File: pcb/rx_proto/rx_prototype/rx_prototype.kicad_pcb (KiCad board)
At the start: 10 copper layers, 3 parts, among them U1 nice_nano, U4 MCP6004, U5 MCP6004

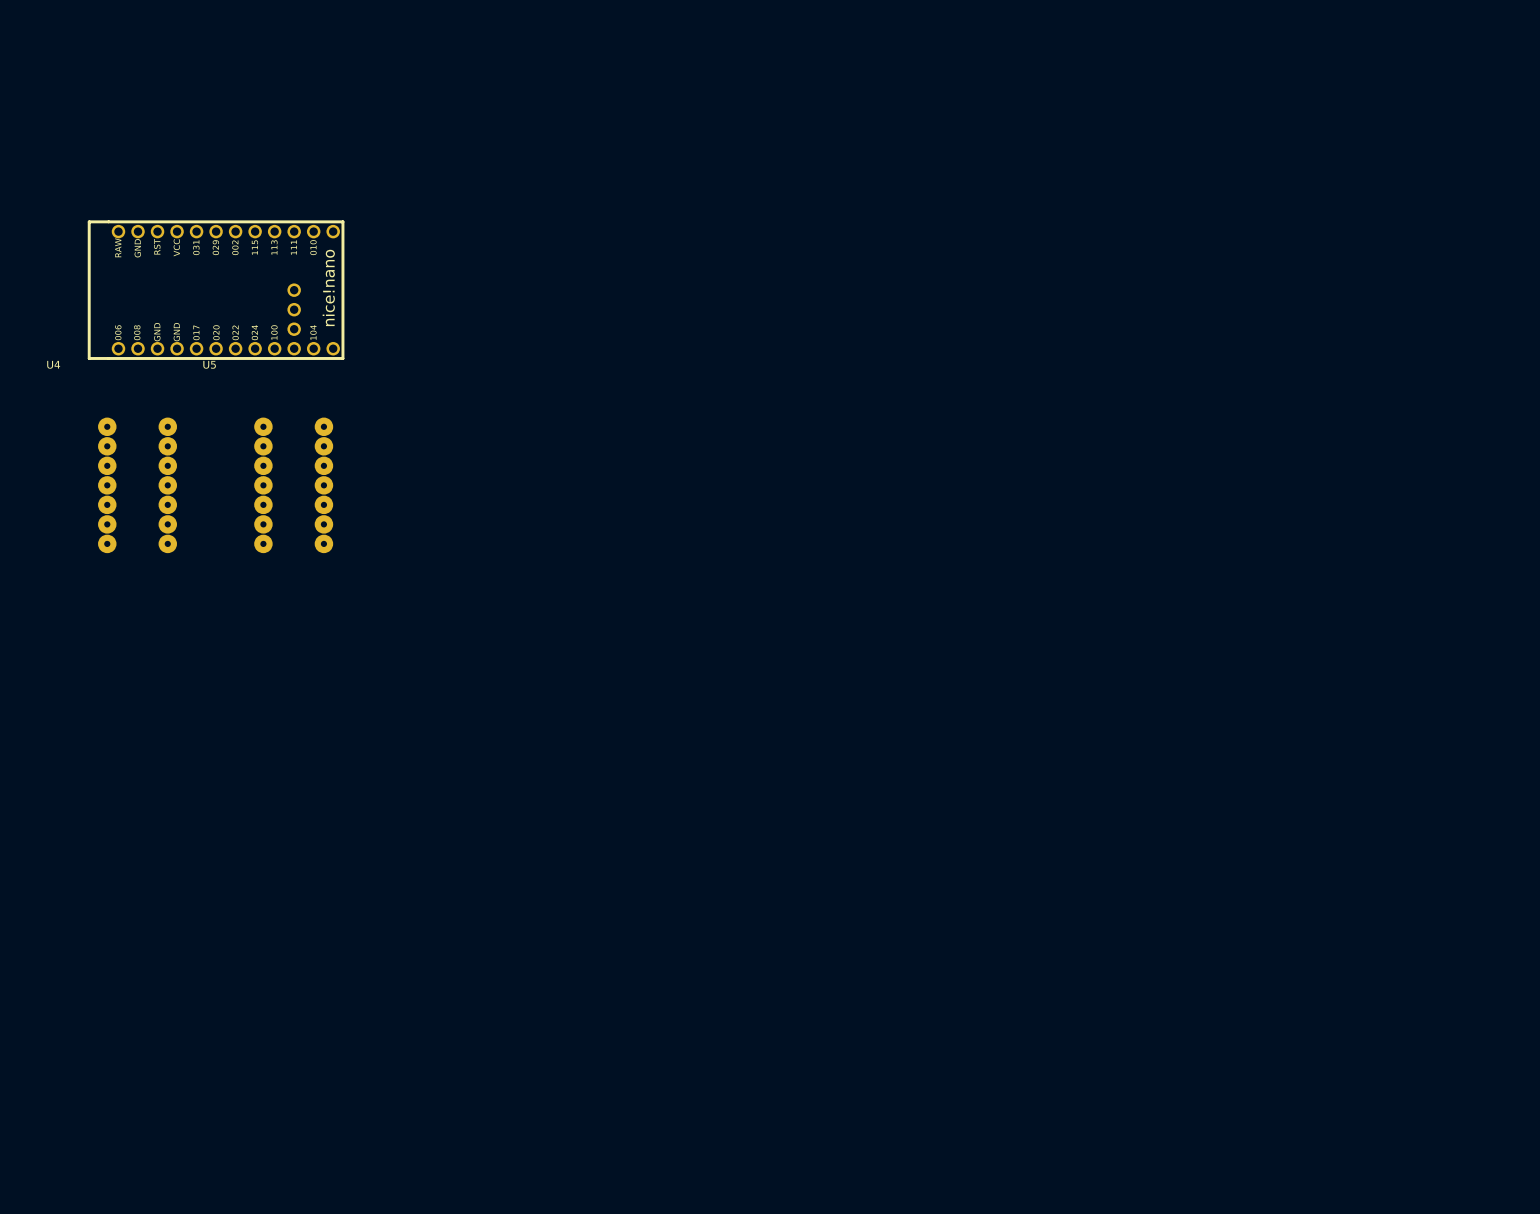
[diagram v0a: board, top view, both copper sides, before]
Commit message: Update perfboard layout
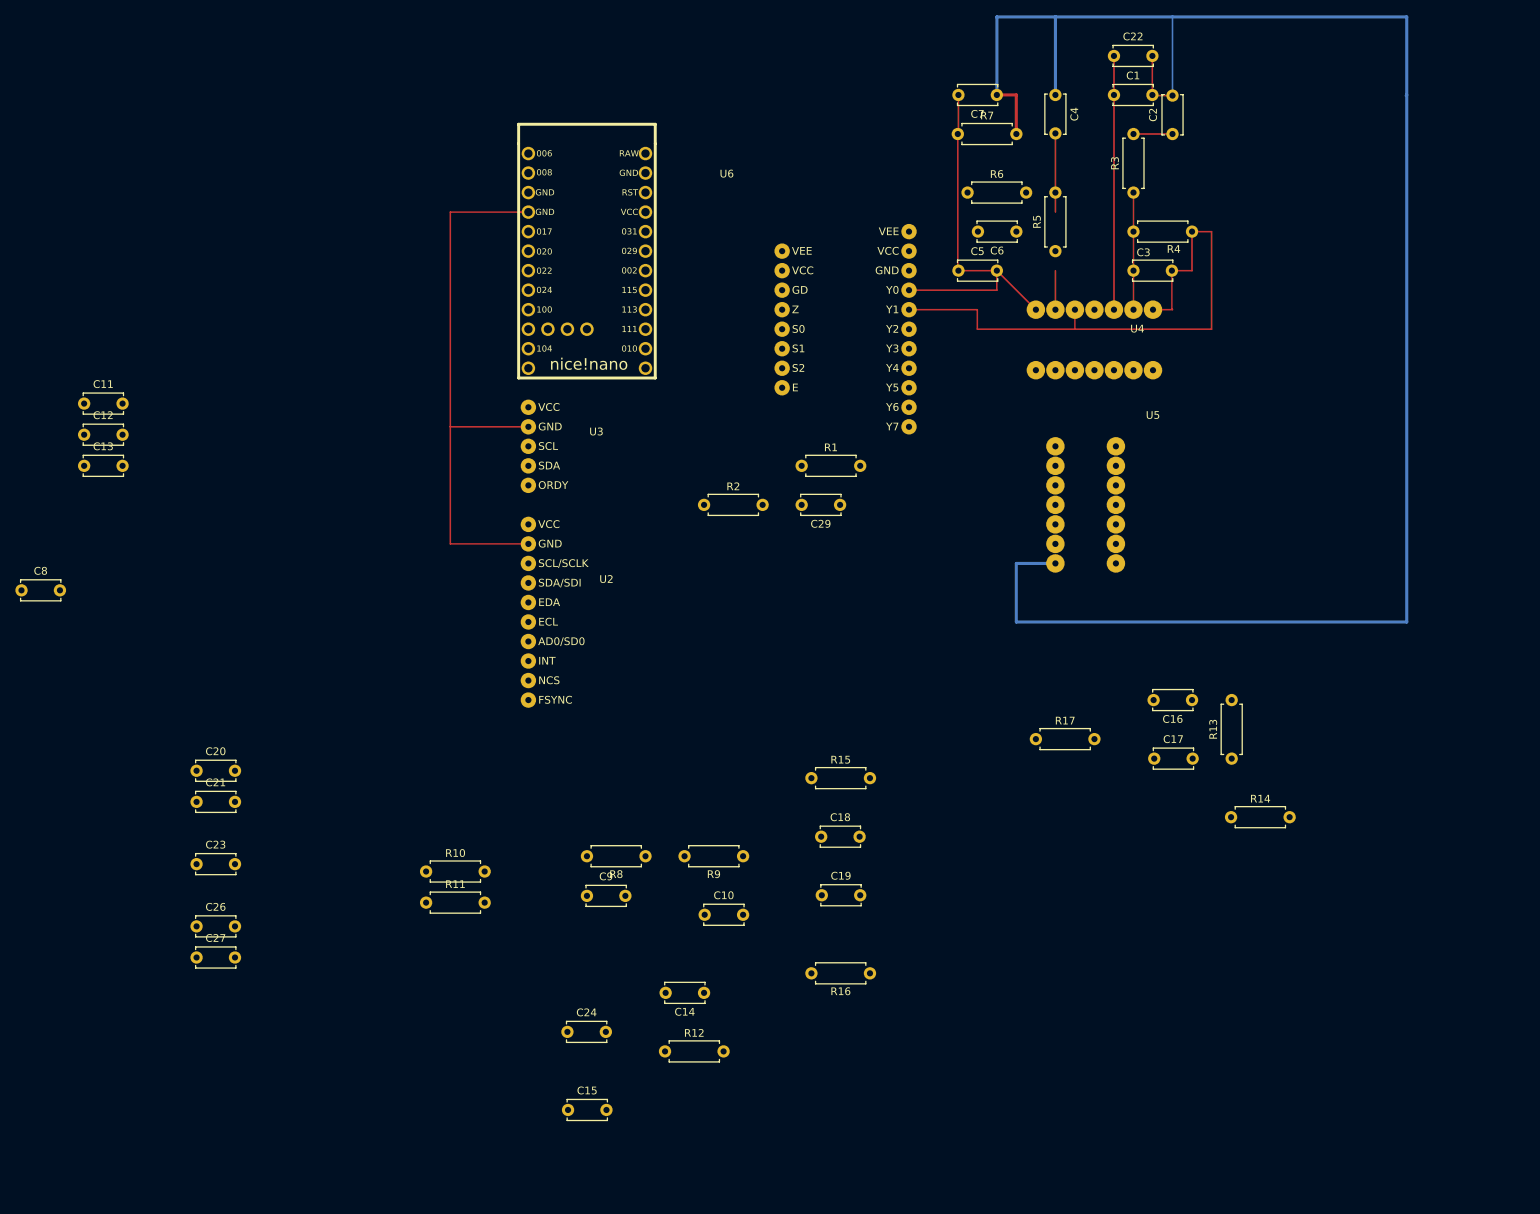
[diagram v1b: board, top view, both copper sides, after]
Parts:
- added C1: 33nF, Capacitor_THT:C_Disc_D5.0mm_W2.5mm_P5.00mm, F.Cu at (203.2, 17.8)
- added C10: 330pF, Capacitor_THT:C_Disc_D5.0mm_W2.5mm_P5.00mm, F.Cu at (149.9, 124.5)
- added C11: 0.1uF, Capacitor_THT:C_Disc_D5.0mm_W2.5mm_P5.00mm, F.Cu at (69.2, 57.9)
- added C12: 330pF, Capacitor_THT:C_Disc_D5.0mm_W2.5mm_P5.00mm, F.Cu at (69.2, 62.0)
- added C13: 100nF, Capacitor_THT:C_Disc_D5.0mm_W2.5mm_P5.00mm, F.Cu at (69.2, 66.0)
- added C14: 1nF, Capacitor_THT:C_Disc_D5.0mm_W2.5mm_P5.00mm, F.Cu at (149.9, 134.6)
- added C15: 10nF, Capacitor_THT:C_Disc_D5.0mm_W2.5mm_P5.00mm, F.Cu at (132.2, 149.9)
- added C16: 47nF, Capacitor_THT:C_Disc_D5.0mm_W2.5mm_P5.00mm, F.Cu at (213.4, 96.5)
- added C17: 330pF, Capacitor_THT:C_Disc_D5.0mm_W2.5mm_P5.00mm, F.Cu at (208.4, 104.1)
- added C18: 0.1uF, Capacitor_THT:C_Disc_D5.0mm_W2.5mm_P5.00mm, F.Cu at (165.1, 114.3)
- added C19: 330pF, Capacitor_THT:C_Disc_D5.0mm_W2.5mm_P5.00mm, F.Cu at (165.2, 121.9)
- added C2: 47nF, Capacitor_THT:C_Disc_D5.0mm_W2.5mm_P5.00mm, F.Cu at (210.8, 22.9)
- added C20: 100nF, Capacitor_THT:C_Disc_D5.0mm_W2.5mm_P5.00mm, F.Cu at (83.8, 105.7)
- added C21: 1nF, Capacitor_THT:C_Disc_D5.0mm_W2.5mm_P5.00mm, F.Cu at (83.8, 109.8)
- added C22: 2.2nf, Capacitor_THT:C_Disc_D5.0mm_W2.5mm_P5.00mm, F.Cu at (203.2, 12.7)
- added C23: 2.2nF, Capacitor_THT:C_Disc_D5.0mm_W2.5mm_P5.00mm, F.Cu at (83.8, 117.9)
- added C24: 2.2nF, Capacitor_THT:C_Disc_D5.0mm_W2.5mm_P5.00mm, F.Cu at (132.1, 139.7)
- added C26: 0.1uF, Capacitor_THT:C_Disc_D5.0mm_W2.5mm_P5.00mm, F.Cu at (83.8, 126.0)
- added C27: 0.1uF, Capacitor_THT:C_Disc_D5.0mm_W2.5mm_P5.00mm, F.Cu at (83.8, 130.0)
- added C29: 0.1uF, Capacitor_THT:C_Disc_D5.0mm_W2.5mm_P5.00mm, F.Cu at (167.6, 71.1)
- added C3: 330pF, Capacitor_THT:C_Disc_D5.0mm_W2.5mm_P5.00mm, F.Cu at (205.7, 40.6)
- added C4: 0.1uF, Capacitor_THT:C_Disc_D5.0mm_W2.5mm_P5.00mm, F.Cu at (195.6, 17.8)
- added C5: 100nF, Capacitor_THT:C_Disc_D5.0mm_W2.5mm_P5.00mm, F.Cu at (183.0, 40.6)
- added C6: 330pF, Capacitor_THT:C_Disc_D5.0mm_W2.5mm_P5.00mm, F.Cu at (190.5, 35.6)
- added C7: 1nF, Capacitor_THT:C_Disc_D5.0mm_W2.5mm_P5.00mm, F.Cu at (188.0, 17.8)
- added C8: 10nF, Capacitor_THT:C_Disc_D5.0mm_W2.5mm_P5.00mm, F.Cu at (61.0, 82.2)
- added C9: 47nF, Capacitor_THT:C_Disc_D5.0mm_W2.5mm_P5.00mm, F.Cu at (134.6, 122.0)
- added R1: 10K, Resistor_THT:R_Axial_DIN0207_L6.3mm_D2.5mm_P7.62mm_Horizontal, F.Cu at (162.6, 66.0)
- added R10: 750, Resistor_THT:R_Axial_DIN0207_L6.3mm_D2.5mm_P7.62mm_Horizontal, F.Cu at (113.7, 118.8)
- added R11: 6.8K, Resistor_THT:R_Axial_DIN0207_L6.3mm_D2.5mm_P7.62mm_Horizontal, F.Cu at (113.7, 122.9)
- added R12: 2.2K, Resistor_THT:R_Axial_DIN0207_L6.3mm_D2.5mm_P7.62mm_Horizontal, F.Cu at (144.8, 142.2)
- added R13: 750, Resistor_THT:R_Axial_DIN0207_L6.3mm_D2.5mm_P7.62mm_Horizontal, F.Cu at (218.5, 104.1)
- added R14: 6.8K, Resistor_THT:R_Axial_DIN0207_L6.3mm_D2.5mm_P7.62mm_Horizontal, F.Cu at (218.4, 111.8)
- added R15: 750, Resistor_THT:R_Axial_DIN0207_L6.3mm_D2.5mm_P7.62mm_Horizontal, F.Cu at (163.8, 106.7)
- added R16: 6.8K, Resistor_THT:R_Axial_DIN0207_L6.3mm_D2.5mm_P7.62mm_Horizontal, F.Cu at (171.4, 132.1)
- added R17: 2.2K, Resistor_THT:R_Axial_DIN0207_L6.3mm_D2.5mm_P7.62mm_Horizontal, F.Cu at (193.0, 101.6)
- added R2: 10K, Resistor_THT:R_Axial_DIN0207_L6.3mm_D2.5mm_P7.62mm_Horizontal, F.Cu at (149.9, 71.1)
- added R3: 750, Resistor_THT:R_Axial_DIN0207_L6.3mm_D2.5mm_P7.62mm_Horizontal, F.Cu at (205.7, 30.5)
- added R4: 6.8K, Resistor_THT:R_Axial_DIN0207_L6.3mm_D2.5mm_P7.62mm_Horizontal, F.Cu at (213.4, 35.6)
- added R5: 750, Resistor_THT:R_Axial_DIN0207_L6.3mm_D2.5mm_P7.62mm_Horizontal, F.Cu at (195.6, 38.1)
- added R6: 6.8K, Resistor_THT:R_Axial_DIN0207_L6.3mm_D2.5mm_P7.62mm_Horizontal, F.Cu at (184.2, 30.5)
- added R7: 2.2K, Resistor_THT:R_Axial_DIN0207_L6.3mm_D2.5mm_P7.62mm_Horizontal, F.Cu at (182.9, 22.9)
- added R8: 750, Resistor_THT:R_Axial_DIN0207_L6.3mm_D2.5mm_P7.62mm_Horizontal, F.Cu at (142.2, 116.8)
- added R9: 6.8K, Resistor_THT:R_Axial_DIN0207_L6.3mm_D2.5mm_P7.62mm_Horizontal, F.Cu at (154.9, 116.8)
- added U2: MPU-6500, Library:MPU-6500, F.Cu at (134.6, 83.3)
- added U3: QMC5883P, Library:QMC5883P, F.Cu at (125.7, 57.1)
- added U6: 74HC4051, Library:74HC4051, F.Cu at (158.8, 33.0)
- moved U4 139.2 mm to (210.8, 45.7), turned to -90 degrees
- moved U5 113.3 mm to (203.5, 81.3), turned to 180 degrees
- moved U1 47.1 mm to (134.6, 39.4), turned to -90 degrees
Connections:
- U1 pad 13: /SELECT_0 -> /SELECT_2
- U1 pad 15: /SELECT_2 -> /SELECT_0
- U1 pad 5: unconnected-(U1-P0.17-Pad5) -> /SDA
- U4 pad 5: Net-(U4B-+) -> /V_OUT1
- U4 pad 7: /V_OUT3 -> Net-(C5-Pad2)
- U5 pad 1: Net-(C5-Pad2) -> /V_OUT3
- U5 pad 10: Net-(U5C-+) -> /ADC_BUFFER
- U5 pad 12: /ADC_BUFFER -> Net-(U5D-+)
- U5 pad 13: /ADC_0 -> /V_BIAS
- U5 pad 14: /ADC_0 -> /V_BIAS
- U5 pad 3: /V_OUT1 -> Net-(U5A-+)
- U5 pad 8: /V_BIAS -> /ADC_0
- U5 pad 9: /V_BIAS -> /ADC_0
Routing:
- net /V_BIAS: track 0.00 -> 244.1 mm
- net GND: track 0.00 -> 231.2 mm
- net +3.3V: track 0.00 -> 161.3 mm
- net /V_OUT1: track 0.00 -> 75.0 mm
- net /SCK: track 0.00 -> 63.5 mm
- net /SDA: track 0.00 -> 61.0 mm
- net Net-(U5D-+): track 0.00 -> 48.3 mm
- net /V_OUT2: track 0.00 -> 41.9 mm
- net Net-(U4A-+): track 0.00 -> 33.0 mm
- net Net-(U4A--): track 0.00 -> 15.2 mm
- net Net-(C4-Pad2): track 0.00 -> 10.2 mm
- net Net-(C5-Pad2): track 0.00 -> 7.02 mm
- net Net-(U4B--): track 0.00 -> 5.08 mm
- net Net-(C2-Pad1): track 0.00 -> 5.08 mm

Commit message: Update perf layout
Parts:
- moved C27 165.5 mm to (216.0, 30.5)
- moved C15 163.5 mm to (243.8, 30.4), turned to 90 degrees
- moved C24 149.2 mm to (233.7, 30.4), turned to 90 degrees
- moved C26 132.9 mm to (213.4, 96.5)
- moved C18 97.3 mm to (238.8, 50.8), turned to 180 degrees
- moved C19 93.3 mm to (231.1, 55.9), turned to -90 degrees
- moved R16 87.7 mm to (226.1, 63.5), turned to 90 degrees
- moved R9 86.4 mm to (240.0, 101.6)
- moved R15 82.0 mm to (223.9, 50.9)
- moved R14 80.2 mm to (233.7, 33.0), turned to -90 degrees
- moved C16 68.1 mm to (243.8, 35.6), turned to -90 degrees
- moved R13 66.6 mm to (238.8, 40.6)
- moved C17 66.6 mm to (228.6, 40.6), turned to 90 degrees
- moved C7 50.1 mm to (203.2, 65.5)
- moved R17 47.6 mm to (227.3, 68.6)
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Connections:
- C10 pad 2: /V_OUT3 -> /V_OUT5
- C13 pad 1: /V_OUT4 -> /V_OUT6
- C14 pad 2: /V_OUT4 -> /V_OUT6
- C15 pad 1: Net-(U4C-+) -> Net-(U4D-+)
- C17 pad 1: Net-(U4C--) -> Net-(U4D--)
- C17 pad 2: /V_OUT5 -> /V_OUT3
- C19 pad 1: Net-(U4D--) -> Net-(U4C--)
- C20 pad 1: /V_OUT6 -> /V_OUT4
- C21 pad 2: /V_OUT6 -> /V_OUT4
- C24 pad 1: Net-(U4C-+) -> Net-(U4D-+)
- R12 pad 1: /V_OUT4 -> /V_OUT6
- R13 pad 1: Net-(U4C--) -> Net-(U4D--)
- R14 pad 1: /V_OUT5 -> /V_OUT3
- R14 pad 2: Net-(U4C--) -> Net-(U4D--)
- R15 pad 1: Net-(U4D--) -> Net-(U4C--)
- R16 pad 2: Net-(U4D--) -> Net-(U4C--)
- R17 pad 1: /V_OUT6 -> /V_OUT4
- R9 pad 1: /V_OUT3 -> /V_OUT5
- U4 pad 10: Net-(U4C-+) -> /V_OUT3
- U4 pad 12: /V_OUT5 -> Net-(U4D-+)
- U4 pad 14: unconnected-(U4-Pad14) -> /V_OUT3
- U4 pad 8: /V_OUT5 -> Net-(C19-Pad2)
- U5 pad 1: /V_OUT3 -> /V_OUT5
- U5 pad 5: /V_OUT3 -> /V_OUT5
- U6 pad 13: /V_OUT2 -> /V_OUT1
- U6 pad 14: /V_OUT1 -> /V_OUT2
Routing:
- net GND: track 231.2 -> 433.4 mm
- net +3.3V: track 161.3 -> 316.5 mm
- net Net-(U4D-+): track 0.00 -> 32.5 mm
- net Net-(U5D-+): track 48.3 -> 78.8 mm
- net /V_OUT3: track 0.00 -> 17.8 mm
- net Net-(U4D--): track 0.00 -> 17.5 mm
- net Net-(U4B--): track 5.08 -> 20.3 mm
- net Net-(C5-Pad2): track 7.02 -> 17.9 mm
- net Net-(C4-Pad2): track 10.2 -> 0.00 mm
- net Net-(U4A-+): track 33.0 -> 25.0 mm
- net Net-(C16-Pad1): track 0.00 -> 7.70 mm
- net Net-(U4A--): track 15.2 -> 22.9 mm
- net /V_BIAS: track 244.1 -> 249.9 mm
- net /V_OUT1: track 75.0 -> 70.0 mm
- net /V_OUT2: track 41.9 -> 46.7 mm

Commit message: Update perf
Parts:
- moved C21 148.7 mm to (208.3, 28.5)
- moved C20 139.7 mm to (203.2, 33.1), turned to -90 degrees
- moved R7 64.7 mm to (243.8, 25.5), turned to 180 degrees
- moved C15 58.6 mm to (195.6, 63.7), turned to -90 degrees
- moved C2 54.8 mm to (246.4, 53.4), turned to -90 degrees
- moved C1 54.5 mm to (241.3, 63.7), turned to -90 degrees
- moved C16 53.4 mm to (195.6, 58.4), turned to 90 degrees
- moved R3 51.5 mm to (241.3, 61.0), turned to 90 degrees
- moved C5 51.4 mm to (241.3, 33.1), turned to -90 degrees
- moved C7 49.5 mm to (236.3, 28.6), turned to 0 degrees
- moved C4 48.7 mm to (243.8, 43.3), turned to 180 degrees
- moved R17 45.3 mm to (213.4, 25.5), turned to 180 degrees
- moved C24 43.4 mm to (205.7, 63.7), turned to -90 degrees
- moved R4 43.3 mm to (236.2, 61.0), turned to 90 degrees
- moved C6 43.2 mm to (236.2, 33.1), turned to -90 degrees
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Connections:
- C17 pad 2: /V_OUT3 -> /V_OUT1
- C20 pad 1: /V_OUT4 -> /V_OUT2
- C21 pad 2: /V_OUT4 -> /V_OUT2
- C3 pad 2: /V_OUT1 -> /V_OUT3
- C5 pad 1: /V_OUT2 -> /V_OUT4
- C7 pad 2: /V_OUT2 -> /V_OUT4
- R14 pad 1: /V_OUT3 -> /V_OUT1
- R17 pad 1: /V_OUT4 -> /V_OUT2
- R4 pad 1: /V_OUT1 -> /V_OUT3
- R7 pad 1: /V_OUT2 -> /V_OUT4
- U4 pad 1: /V_OUT1 -> /V_OUT3
- U4 pad 10: /V_OUT3 -> /V_OUT1
- U4 pad 14: /V_OUT3 -> /V_OUT1
- U4 pad 5: /V_OUT1 -> /V_OUT3
- U6 pad 12: /V_OUT4 -> /V_OUT3
- U6 pad 13: /V_OUT1 -> /V_OUT2
- U6 pad 14: /V_OUT2 -> /V_OUT1
- U6 pad 15: /V_OUT3 -> /V_OUT4
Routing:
- net /V_OUT3: track 17.8 -> 133.5 mm
- net /V_OUT4: track 0.00 -> 110.3 mm
- net Net-(U5D-+): track 78.8 -> 33.1 mm
- net Net-(U4C--): track 0.00 -> 18.2 mm
- net Net-(C19-Pad2): track 0.00 -> 17.6 mm
- net /V_OUT1: track 70.0 -> 87.4 mm
- net +3.3V: track 316.5 -> 326.5 mm
- net /V_BIAS: track 249.9 -> 240.8 mm
- net /V_OUT2: track 46.7 -> 54.7 mm
- net Net-(C18-Pad2): track 0.00 -> 2.26 mm
- net GND: track 433.4 -> 432.3 mm
